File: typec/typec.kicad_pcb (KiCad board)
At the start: 2 copper layers, 17 parts, among them U1 TPD6E05U06-USON, U2 TPD4E05U06-USON, U3 TPS62081-WSON, U4 TPD4E05U06-USON, U5 TPS74801-VSON

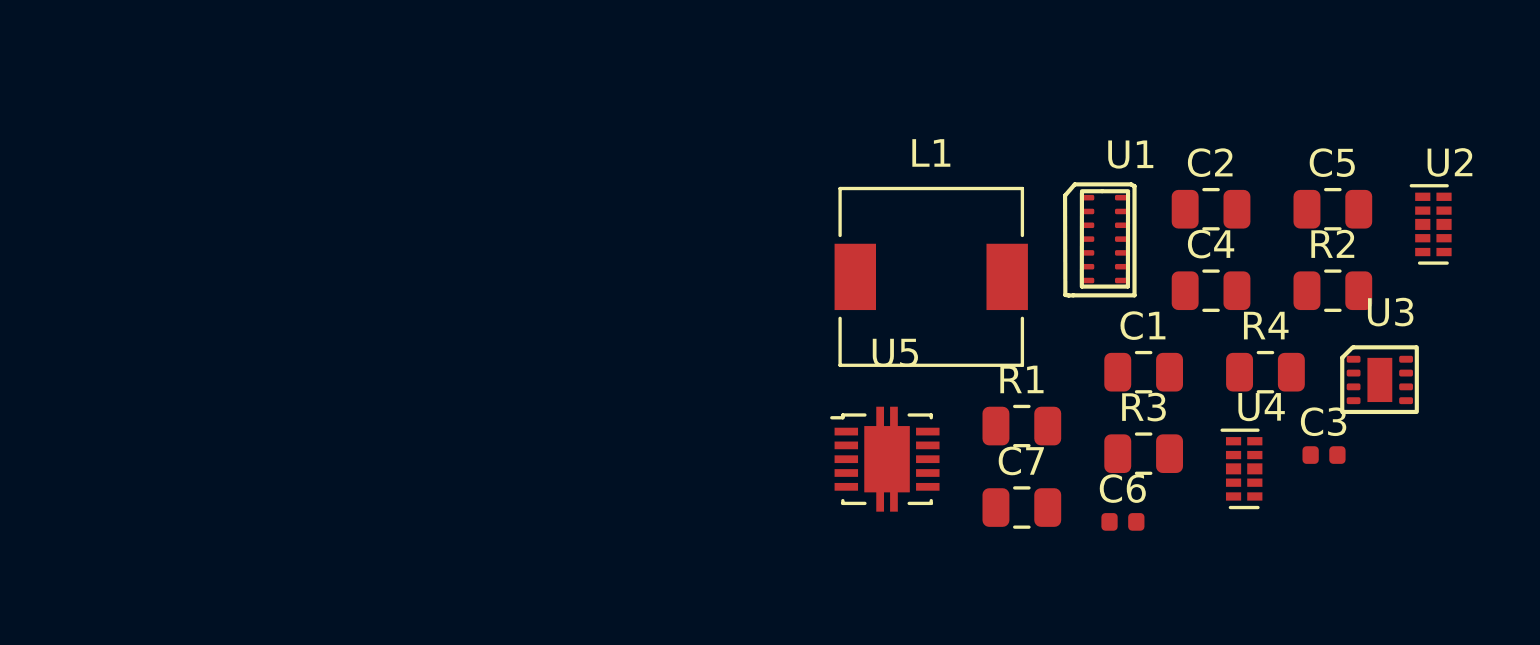
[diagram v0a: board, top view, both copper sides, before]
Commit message: Added TUSB212 and USB 3.1 Connector
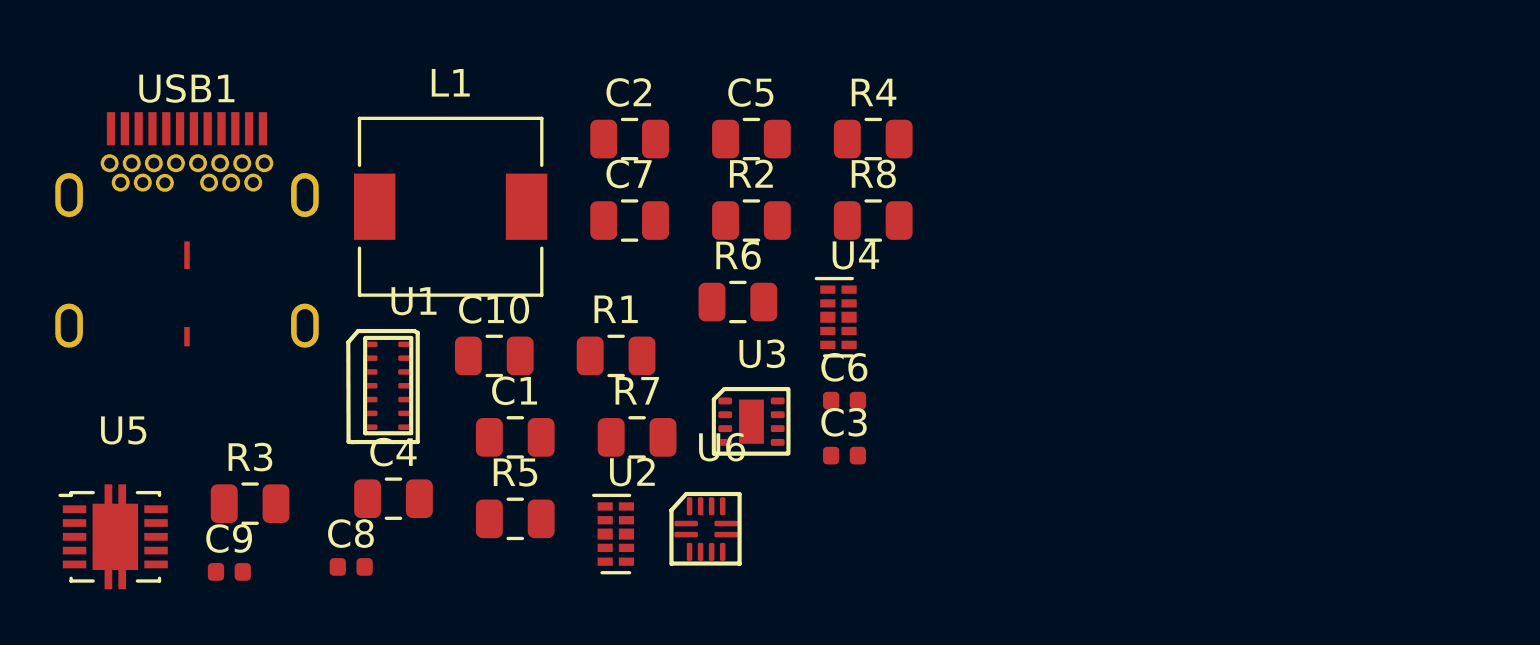
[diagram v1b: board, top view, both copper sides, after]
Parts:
- added C10: 10uf/10v, Capacitor_SMD:C_0805_2012Metric, F.Cu at (108.6, 96.5)
- added C8: 0.1uF/10v, Capacitor_SMD:C_0402_1005Metric, F.Cu at (103.4, 104.1)
- added C9: 0.1uF/10v, Capacitor_SMD:C_0402_1005Metric, F.Cu at (99.0, 104.3)
- added R5: 1.6K, Resistor_SMD:R_0805_2012Metric, F.Cu at (109.4, 102.4)
- added R6: 43K, Resistor_SMD:R_0805_2012Metric, F.Cu at (117.4, 94.5)
- added R7: 0 E, Resistor_SMD:R_0805_2012Metric, F.Cu at (113.8, 99.4)
- added R8: 0 E, Resistor_SMD:R_0805_2012Metric, F.Cu at (122.3, 91.6)
- added U6: TUSB212-X2QFN, TUSB212-X2QFN:TUSB212-X2QFN, F.Cu at (116.3, 102.7)
- added USB1: Wurth-632723300011, Type-C:Wurth-632723300011-MaximumExtensionMount, F.Cu at (97.5, 98.8)
- moved R3 32.4 mm to (99.8, 101.8)
- moved U2 31.7 mm to (112.7, 103.0)
- moved C4 30.5 mm to (105.0, 101.6)
- moved U5 28.1 mm to (94.4, 102.8)
- moved U1 26.5 mm to (104.8, 97.5)
- moved C1 22.9 mm to (109.4, 99.4)
- moved U3 22.8 mm to (117.6, 99.2)
- moved C2 21.2 mm to (113.5, 88.6)
- moved C5 21.2 mm to (117.9, 88.6)
- moved R2 21.2 mm to (117.9, 91.6)
- moved C7 17.6 mm to (113.5, 91.6)
- moved L1 17.6 mm to (107.0, 91.1)
- moved C3 17.4 mm to (121.3, 100.1)
- moved R4 16.5 mm to (122.3, 88.6)
- moved U4 15.7 mm to (120.7, 95.1)
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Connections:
- C7 pad 1: Net-(C7-Pad1) -> VOUT(3.3V)
- U3 pad 3: Net-(U3-Pad3) -> GND
- U3 pad 4: Net-(U3-Pad4) -> GND
- U3 pad 8: Net-(U3-Pad8) -> VBUS

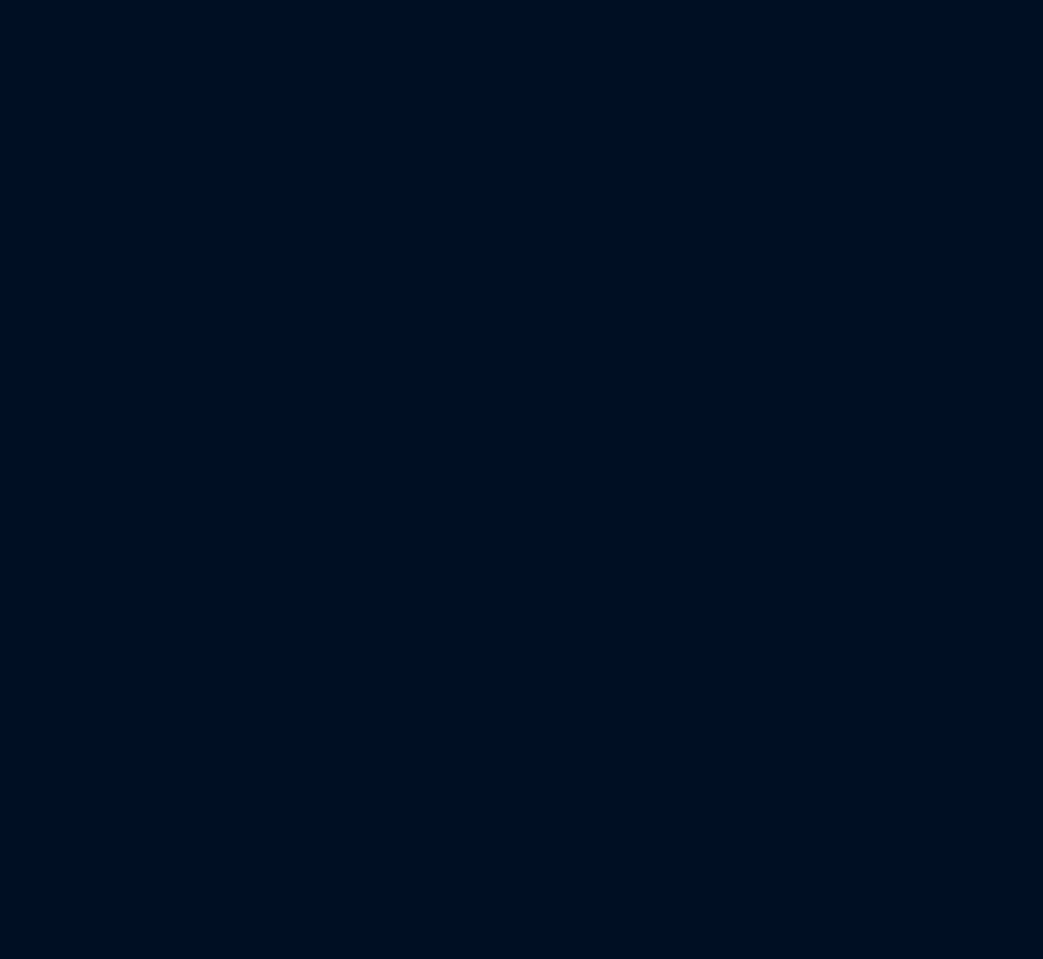
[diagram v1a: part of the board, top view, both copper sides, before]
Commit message: Added another page and completed the Multiplexer schematics.
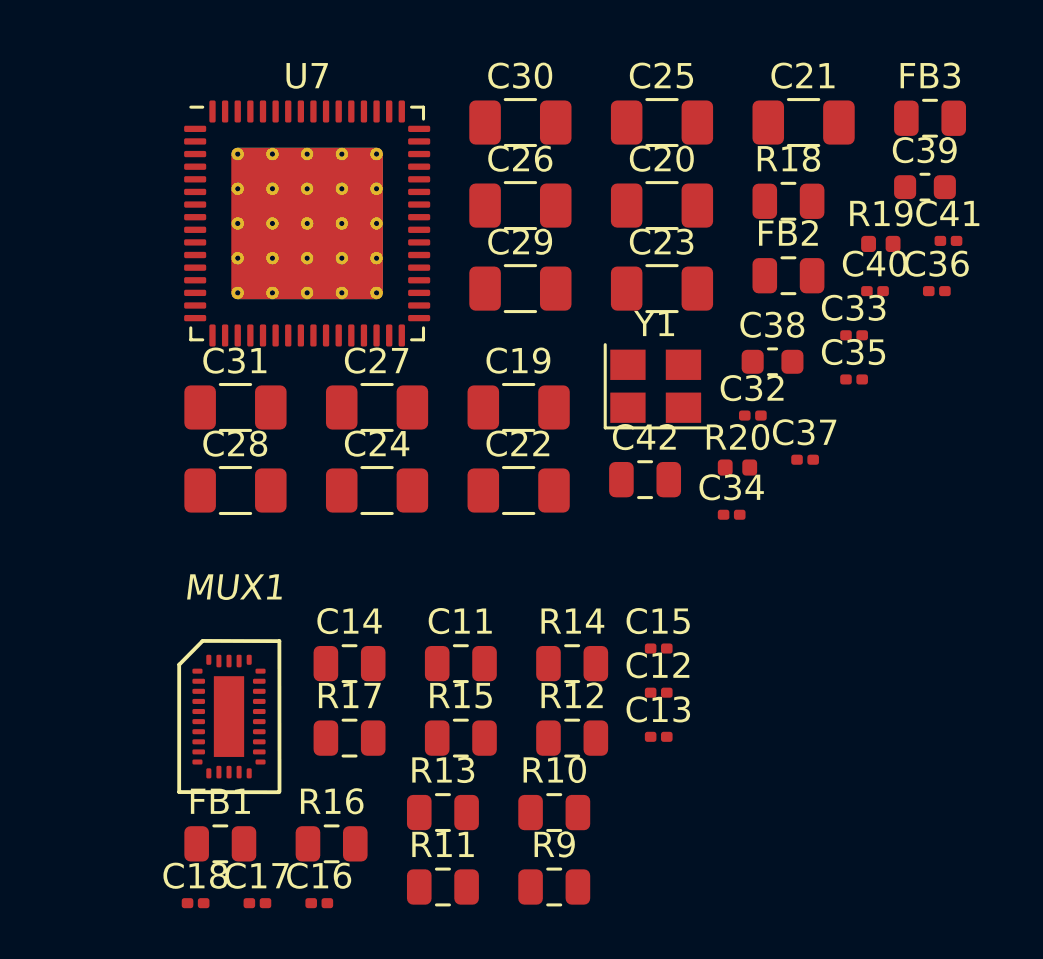
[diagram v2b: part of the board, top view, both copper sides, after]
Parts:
- added C11: 0.1uf/10v, Capacitor_SMD:C_0805_2012Metric, F.Cu at (152.2, 100.1)
- added C12: 0.47uf/10v, Capacitor_SMD:C_0201_0603Metric, F.Cu at (160.0, 101.2)
- added C13: 0.47uf/10v, Capacitor_SMD:C_0201_0603Metric, F.Cu at (160.0, 103.0)
- added C14: 47uf/10v, Capacitor_SMD:C_0805_2012Metric, F.Cu at (147.8, 100.1)
- added C15: 0.4uf/10v, Capacitor_SMD:C_0201_0603Metric, F.Cu at (160.0, 99.5)
- added C16: 0.47uf/10v, Capacitor_SMD:C_0201_0603Metric, F.Cu at (146.6, 109.5)
- added C17: 0.4uf/10v, Capacitor_SMD:C_0201_0603Metric, F.Cu at (144.1, 109.5)
- added C18: 0.4uf/10v, Capacitor_SMD:C_0201_0603Metric, F.Cu at (141.7, 109.5)
- added C19: 0.1uF/10v, Capacitor_SMD:C_1206_3216Metric, F.Cu at (154.5, 89.9)
- added C20: 0.1uF/10v, Capacitor_SMD:C_1206_3216Metric, F.Cu at (160.2, 81.9)
- added C21: 0.1uF/10v, Capacitor_SMD:C_1206_3216Metric, F.Cu at (165.8, 78.6)
- added C22: 0.1uF/10v, Capacitor_SMD:C_1206_3216Metric, F.Cu at (154.5, 93.2)
- added C23: 0.1uF/10v, Capacitor_SMD:C_1206_3216Metric, F.Cu at (160.2, 85.2)
- added C24: 0.1uF/10v, Capacitor_SMD:C_1206_3216Metric, F.Cu at (148.9, 93.2)
- added C25: 0.1uF/10v, Capacitor_SMD:C_1206_3216Metric, F.Cu at (160.2, 78.6)
- added C26: 10uF/10v, Capacitor_SMD:C_1206_3216Metric, F.Cu at (154.6, 81.9)
- added C27: 0.1uF/10v, Capacitor_SMD:C_1206_3216Metric, F.Cu at (148.9, 89.9)
- added C28: 0.1uF/10v, Capacitor_SMD:C_1206_3216Metric, F.Cu at (143.3, 93.2)
- added C29: 0.1uF/10v, Capacitor_SMD:C_1206_3216Metric, F.Cu at (154.6, 85.2)
- added C30: 0.1uF/10v, Capacitor_SMD:C_1206_3216Metric, F.Cu at (154.6, 78.6)
- added C31: 10uF/10v, Capacitor_SMD:C_1206_3216Metric, F.Cu at (143.3, 89.9)
- added C32: 0.1uF/10v, Capacitor_SMD:C_0201_0603Metric, F.Cu at (163.8, 90.2)
- added C33: 0.1uF/10v, Capacitor_SMD:C_0201_0603Metric, F.Cu at (167.8, 87.0)
- added C34: 0.1uF/10v, Capacitor_SMD:C_0201_0603Metric, F.Cu at (162.9, 94.2)
- added C35: 0.1uF/10v, Capacitor_SMD:C_0201_0603Metric, F.Cu at (167.8, 88.8)
- added C36: 0.1uF/10v, Capacitor_SMD:C_0201_0603Metric, F.Cu at (171.1, 85.3)
- added C37: 0.1uF/10v, Capacitor_SMD:C_0201_0603Metric, F.Cu at (165.8, 92.0)
- added C38: 18pF/10v, Capacitor_SMD:C_0603_1608Metric, F.Cu at (164.6, 88.1)
- added C39: 18pF/10v, Capacitor_SMD:C_0603_1608Metric, F.Cu at (170.6, 81.2)
- added C40: 0.1uF/10v, Capacitor_SMD:C_0201_0603Metric, F.Cu at (168.6, 85.3)
- added C41: 0.1uF/10v, Capacitor_SMD:C_0201_0603Metric, F.Cu at (171.5, 83.3)
- added C42: 1uF/10v, Capacitor_SMD:C_0805_2012Metric, F.Cu at (159.5, 92.8)
- added FB1: Ferrite_Bead, Inductor_SMD:L_0805_2012Metric, F.Cu at (142.7, 107.2)
- added FB2: Ferrite_Bead, Inductor_SMD:L_0805_2012Metric, F.Cu at (165.2, 84.7)
- added FB3: Ferrite_Bead, Inductor_SMD:L_0805_2012Metric, F.Cu at (170.8, 78.4)
- added MUX1: HD3SS3220, HD3SS3220-VQFN:HD3SS3220-VQFN-MUX, F.Cu at (143.0, 102.2)
- added R10: 10 K, Resistor_SMD:R_0805_2012Metric, F.Cu at (155.9, 106.0)
- added R11: 900 K, Resistor_SMD:R_0805_2012Metric, F.Cu at (151.5, 108.9)
- added R12: 100K, Resistor_SMD:R_0805_2012Metric, F.Cu at (156.6, 103.0)
- added R13: 4.7K, Resistor_SMD:R_0805_2012Metric, F.Cu at (151.5, 106.0)
- added R14: 100K, Resistor_SMD:R_0805_2012Metric, F.Cu at (156.6, 100.1)
- added R15: 100K, Resistor_SMD:R_0805_2012Metric, F.Cu at (152.2, 103.0)
- added R16: 0 E, Resistor_SMD:R_0805_2012Metric, F.Cu at (147.1, 107.2)
- added R17: 0 E, Resistor_SMD:R_0805_2012Metric, F.Cu at (147.8, 103.0)
- added R18: 1 M, Resistor_SMD:R_0805_2012Metric, F.Cu at (165.2, 81.7)
- added R19: 4.7K, Resistor_SMD:R_0402_1005Metric, F.Cu at (168.8, 83.4)
- added R20: 4.7K, Resistor_SMD:R_0402_1005Metric, F.Cu at (163.2, 92.3)
- added R9: 100K, Resistor_SMD:R_0805_2012Metric, F.Cu at (155.9, 108.9)
- added U7: USB_HUB, TUSB8042-VQFN:QFN-64-1EP_9x9mm_P0.5mm_EP6x6mm_ThermalVias, F.Cu at (146.1, 82.6)
- added Y1: 24 MHz, Crystal:Crystal_SMD_3225-4Pin_3.2x2.5mm, F.Cu at (159.9, 89.1)
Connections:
- net GND renamed USB3_RX0N
- USB1 pad 15: CRX2N -> CTX2N

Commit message: Last minute changes
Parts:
- moved C9 57.8 mm to (154.3, 87.4)
- moved C8 54.2 mm to (154.3, 85.4)
- moved C1 50.4 mm to (155.3, 78.9)
- moved R3 49.7 mm to (146.0, 83.8)
- moved C17 47.9 mm to (180.9, 78.8)
- moved C4 47.4 mm to (146.5, 78.9)
- moved C16 47.2 mm to (180.9, 77.1)
- moved FB1 46.8 mm to (177.5, 75.9)
- moved C10 43.1 mm to (146.5, 75.9)
- moved C25 42.9 mm to (133.6, 112.3)
- moved FB3 42.7 mm to (144.3, 111.8)
- moved C29 37.9 mm to (128.0, 112.3)
- moved C36 36.4 mm to (147.7, 113.2)
- moved L1 35.4 mm to (140.0, 78.4)
- moved C5 35.4 mm to (150.9, 75.9)
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
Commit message: updated
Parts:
- removed C37: 0.1uF/10v, Capacitor_SMD:C_0201_0603Metric
- removed C9: 0.1uF/10v, Capacitor_SMD:C_0402_1005Metric
- added C43: 1uF/10v, Capacitor_SMD:C_0603_1608Metric, F.Cu at (148.6, 66.8)
- added C44: 1uf/10v, Capacitor_SMD:C_0603_1608Metric, F.Cu at (153.8, 65.4)
- added C45: 1uf/10v, Capacitor_SMD:C_0603_1608Metric, F.Cu at (153.7, 67.3)
- added C46: 10 uF/10v, Capacitor_SMD:C_0603_1608Metric, F.Cu at (152.0, 69.0)
- added D1: LED, LED_SMD:LED_0402_1005Metric, F.Cu at (148.8, 54.7)
- added D10: LED, LED_SMD:LED_0402_1005Metric, F.Cu at (138.4, 93.6)
- added D11: LED, LED_SMD:LED_0402_1005Metric, F.Cu at (138.5, 91.3)
- added D12: LED, LED_SMD:LED_0402_1005Metric, F.Cu at (138.5, 89.3)
- added D2: LED, LED_SMD:LED_0402_1005Metric, F.Cu at (157.5, 51.3)
- added D3: LED, LED_SMD:LED_0402_1005Metric, F.Cu at (148.9, 53.0)
- added D4: LED, LED_SMD:LED_0402_1005Metric, F.Cu at (134.0, 64.8)
- added D5: LED, LED_SMD:LED_0402_1005Metric, F.Cu at (132.0, 38.0)
- added D6: LED, LED_SMD:LED_0402_1005Metric, F.Cu at (130.7, 52.5)
- added D7: LED, LED_SMD:LED_0402_1005Metric, F.Cu at (137.9, 52.1)
- added D8: LED, LED_SMD:LED_0402_1005Metric, F.Cu at (134.6, 60.6)
- added D9: LED, LED_SMD:LED_0402_1005Metric, F.Cu at (159.1, 72.9)
- added J1: Conn_01x05_Female, Connector_JST:JST_GH_SM05B-GHS-TB_1x05-1MP_P1.25mm_Horizontal, F.Cu at (117.3, 94.7)
- added J2: Conn_01x05_Female, Connector_JST:JST_GH_SM05B-GHS-TB_1x05-1MP_P1.25mm_Horizontal, F.Cu at (116.9, 57.5)
- added J3: Conn_01x05_Female, Connector_JST:JST_GH_SM05B-GHS-TB_1x05-1MP_P1.25mm_Horizontal, F.Cu at (117.2, 69.4)
- added J4: Conn_01x05_Female, Connector_JST:JST_GH_SM05B-GHS-TB_1x05-1MP_P1.25mm_Horizontal, F.Cu at (117.3, 81.8)
- added J5: Conn_01x05_Female, Connector_JST:JST_GH_SM05B-GHS-TB_1x05-1MP_P1.25mm_Horizontal, F.Cu at (131.9, 102.4)
- added J6: Conn_01x02_Female, Connector_PinHeader_1.00mm:PinHeader_1x02_P1.00mm_Vertical, F.Cu at (156.6, 95.9)
- added JP1: Jumper_NO_Small, Connector_PinHeader_1.00mm:PinHeader_1x02_P1.00mm_Vertical, F.Cu at (153.4, 48.8)
- added JP2: Jumper_NO_Small, Connector_PinHeader_1.00mm:PinHeader_1x02_P1.00mm_Vertical, F.Cu at (158.4, 48.7)
- added JP3: Jumper_3_Open, Connector_JST:JST_EH_B3B-EH-A_1x03_P2.50mm_Vertical, F.Cu at (161.8, 36.2)
- added JP4: Jumper_2_Open, Connector_PinHeader_1.00mm:PinHeader_1x02_P1.00mm_Vertical, F.Cu at (151.5, 63.4)
- added JP5: Jumper_2_Open, Connector_PinHeader_1.00mm:PinHeader_1x02_P1.00mm_Vertical, F.Cu at (146.6, 63.9)
- added JP6: Jumper_2_Open, Connector_PinHeader_1.00mm:PinHeader_1x02_P1.00mm_Vertical, F.Cu at (150.9, 60.7)
- added JP7: Jumper_2_Open, Connector_PinHeader_1.00mm:PinHeader_1x02_P1.00mm_Vertical, F.Cu at (148.0, 61.4)
- added JP8: Jumper_3_Open, Connector_JST:JST_EH_B3B-EH-A_1x03_P2.50mm_Vertical, F.Cu at (115.5, 38.7)
- added JP9: Jumper_3_Open, Connector_JST:JST_EH_B3B-EH-A_1x03_P2.50mm_Vertical, F.Cu at (116.3, 46.3)
- added R21: 0 E, Resistor_SMD:R_0201_0603Metric, F.Cu at (147.0, 55.1)
- added R22: 200 K, Resistor_SMD:R_0402_1005Metric, F.Cu at (138.1, 59.0)
- added R23: 500 E, Resistor_SMD:R_0402_1005Metric, F.Cu at (136.1, 51.9)
- added R25: 200 K, Resistor_SMD:R_0402_1005Metric, F.Cu at (151.4, 57.7)
- added R26: 500 E, Resistor_SMD:R_0402_1005Metric, F.Cu at (136.3, 60.2)
- added R27: NC / 10 K, Resistor_SMD:R_0402_1005Metric, F.Cu at (124.8, 67.5)
- added R28: NC/ 10 K, Resistor_SMD:R_0402_1005Metric, F.Cu at (125.5, 63.5)
- added R31: 330 E, Resistor_SMD:R_0402_1005Metric, F.Cu at (160.3, 73.9)
- added R34: 330 E, Resistor_SMD:R_0402_1005Metric, F.Cu at (141.2, 64.6)
- added R35: 330 E, Resistor_SMD:R_0402_1005Metric, F.Cu at (154.7, 74.2)
- added R36: 330 E, Resistor_SMD:R_0402_1005Metric, F.Cu at (135.2, 90.6)
- added R37: 1 K, Resistor_SMD:R_0402_1005Metric, F.Cu at (173.3, 75.3)
- added R38: 1 K, Resistor_SMD:R_0402_1005Metric, F.Cu at (172.6, 82.1)
- added R39: 1 K, Resistor_SMD:R_0402_1005Metric, F.Cu at (172.4, 84.6)
- added R40: 9.53 K, Resistor_SMD:R_0402_1005Metric, F.Cu at (139.8, 66.5)
- added R41: 1 K, Resistor_SMD:R_0402_1005Metric, F.Cu at (130.9, 89.5)
- added R43: 1 K, Resistor_SMD:R_0402_1005Metric, F.Cu at (172.5, 80.1)
- added R44: 1 M, Resistor_SMD:R_0402_1005Metric, F.Cu at (125.8, 80.6)
- added R45: 1 K, Resistor_SMD:R_0402_1005Metric, F.Cu at (180.0, 103.7)
- added R46: 1 K, Resistor_SMD:R_0402_1005Metric, F.Cu at (175.1, 103.6)
- added R47: 1 K, Resistor_SMD:R_0402_1005Metric, F.Cu at (177.6, 103.7)
- added R48: 10 K, Resistor_SMD:R_0402_1005Metric, F.Cu at (172.8, 58.7)
- added R49: 1 K, Resistor_SMD:R_0402_1005Metric, F.Cu at (172.9, 104.2)
- added R50: 10 K, Resistor_SMD:R_0402_1005Metric, F.Cu at (172.6, 61.3)
- added R51: 4.7 K, Resistor_SMD:R_0402_1005Metric, F.Cu at (169.9, 103.6)
- added R52: 10 K, Resistor_SMD:R_0402_1005Metric, F.Cu at (172.7, 63.8)
- added R53: 4.7 K, Resistor_SMD:R_0402_1005Metric, F.Cu at (167.4, 103.6)
- added R54: 90.9 K, Resistor_SMD:R_0402_1005Metric, F.Cu at (151.7, 70.9)
- added R55: 10 K, Resistor_SMD:R_0402_1005Metric, F.Cu at (172.7, 66.4)
- added R56: 10 K, Resistor_SMD:R_0402_1005Metric, F.Cu at (154.6, 69.3)
- added R57: 4.7 K, Resistor_SMD:R_0402_1005Metric, F.Cu at (165.0, 103.6)
- added R58: 4.7 K, Resistor_SMD:R_0402_1005Metric, F.Cu at (174.5, 64.6)
- added SW1: SW_Push_Dual_x2, Button_Switch_THT:SW_DIP_SPSTx01_Slide_6.7x4.1mm_W7.62mm_P2.54mm_LowProfile, F.Cu at (163.0, 47.7)
- added SW2: SW_DIP_x06, Button_Switch_THT:SW_DIP_SPSTx06_Slide_6.7x16.8mm_W7.62mm_P2.54mm_LowProfile, F.Cu at (162.5, 72.0)
- added SW4: SW_DIP_x08, Button_Switch_THT:SW_DIP_SPSTx08_Slide_6.7x21.88mm_W7.62mm_P2.54mm_LowProfile, F.Cu at (180.1, 93.9)
- added SW5: SW_DIP_x04, Button_Switch_THT:SW_DIP_SPSTx04_Slide_6.7x11.72mm_W7.62mm_P2.54mm_LowProfile, F.Cu at (162.6, 59.4)
- added TP1: TestPoint, TestPoint:TestPoint_THTPad_2.0x2.0mm_Drill1.0mm, F.Cu at (152.9, 35.3)
- added TP2: TestPoint, TestPoint:TestPoint_THTPad_2.0x2.0mm_Drill1.0mm, F.Cu at (125.9, 36.0)
- added TP3: TestPoint, TestPoint:TestPoint_THTPad_2.0x2.0mm_Drill1.0mm, F.Cu at (129.9, 60.5)
- added TP4: TestPoint, TestPoint:TestPoint_THTPad_2.0x2.0mm_Drill1.0mm, F.Cu at (128.8, 48.1)
- added TP5: TestPoint, TestPoint:TestPoint_THTPad_2.0x2.0mm_Drill1.0mm, F.Cu at (125.2, 51.1)
- added TP6: TestPoint, TestPoint:TestPoint_THTPad_2.0x2.0mm_Drill1.0mm, F.Cu at (178.4, 81.7)
- added TP7: TestPoint, TestPoint:TestPoint_THTPad_2.0x2.0mm_Drill1.0mm, F.Cu at (162.3, 104.3)
- added TP8: TestPoint, TestPoint:TestPoint_THTPad_2.0x2.0mm_Drill1.0mm, F.Cu at (128.1, 89.0)
- added e1: 105 K, Resistor_SMD:R_0201_0603Metric, F.Cu at (134.1, 67.5)
- C10: value 10uf/10v -> 0.1uf/10v; footprint Capacitor_SMD:C_0805_2012Metric -> Capacitor_SMD:C_0603_1608Metric
- C11: value 0.1uf/10v -> 0.47uf/10v; footprint Capacitor_SMD:C_0805_2012Metric -> Capacitor_SMD:C_0201_0603Metric
- C13: value 0.47uf/10v -> 4.7uf/10v; footprint Capacitor_SMD:C_0201_0603Metric -> Capacitor_SMD:C_0402_1005Metric
- C14: value 47uf/10v -> 0.4uf/10v; footprint Capacitor_SMD:C_0805_2012Metric -> Capacitor_SMD:C_0201_0603Metric
- C15: value 0.4uf/10v -> 0.47uf/10v
- C16: value 0.47uf/10v -> 0.4uf/10v
- C18: value 0.4uf/10v -> 10uF/10v; footprint Capacitor_SMD:C_0201_0603Metric -> Capacitor_SMD:C_0603_1608Metric
- C19, C20, C21, C22, C23, C24, C25, C28, C29, C30: footprint Capacitor_SMD:C_1206_3216Metric -> Capacitor_SMD:C_0402_1005Metric
- C2: value 10uf/10v -> 0.1uF/10v; footprint Capacitor_SMD:C_0805_2012Metric -> Capacitor_SMD:C_0402_1005Metric
- C26: value 10uF/10v -> 0.1uF/10v; footprint Capacitor_SMD:C_1206_3216Metric -> Capacitor_SMD:C_0603_1608Metric
- C27: footprint Capacitor_SMD:C_1206_3216Metric -> Capacitor_SMD:C_0603_1608Metric
- C3: value 1uf/10v -> 10uf/10v
- C31: value 10uF/10v -> 0.1uF/10v; footprint Capacitor_SMD:C_1206_3216Metric -> Capacitor_SMD:C_0402_1005Metric
- C32, C33: footprint Capacitor_SMD:C_0201_0603Metric -> Capacitor_SMD:C_0603_1608Metric
- C34: value 0.1uF/10v -> 10uF/10v; footprint Capacitor_SMD:C_0201_0603Metric -> Capacitor_SMD:C_0603_1608Metric
- C35, C41: footprint Capacitor_SMD:C_0201_0603Metric -> Capacitor_SMD:C_0402_1005Metric
- C36: value 0.1uF/10v -> 1uf/10v; footprint Capacitor_SMD:C_0201_0603Metric -> Capacitor_SMD:C_0603_1608Metric
- C38: value 18pF/10v -> 0.1uF/10v; footprint Capacitor_SMD:C_0603_1608Metric -> Capacitor_SMD:C_0402_1005Metric
- C39: footprint Capacitor_SMD:C_0603_1608Metric -> Capacitor_SMD:C_0402_1005Metric
- C4: value 10 uF/10V -> 1uf/10v; footprint Capacitor_SMD:C_0805_2012Metric -> Capacitor_SMD:C_0603_1608Metric
- C40: value 0.1uF/10v -> 18pF/10v; footprint Capacitor_SMD:C_0201_0603Metric -> Capacitor_SMD:C_0402_1005Metric
- C42: value 1uF/10v -> 0.1uF/10v; footprint Capacitor_SMD:C_0805_2012Metric -> Capacitor_SMD:C_0402_1005Metric
- C5: value 22uf/6.3v -> 10 uF/10V; footprint Capacitor_SMD:C_0805_2012Metric -> Capacitor_SMD:C_0603_1608Metric
- C6: value 560pf/10v -> 590pf/10v; footprint Capacitor_SMD:C_0402_1005Metric -> Capacitor_SMD:C_0201_0603Metric
- C7: value 10uf/10v -> 22uf/6.3v; footprint Capacitor_SMD:C_0805_2012Metric -> Capacitor_SMD:C_0603_1608Metric
- C8: value 0.1uF/10v -> 10uf/10v; footprint Capacitor_SMD:C_0402_1005Metric -> Capacitor_SMD:C_0603_1608Metric
- L1: footprint Inductor_SMD:L_6.3x6.3_H3 -> Inductor_SMD:L_Wuerth_MAPI-3015
- R1: value 105 K -> 1.6K; footprint Resistor_SMD:R_0805_2012Metric -> Resistor_SMD:R_0201_0603Metric
- R10: value 10 K -> 1.9K; footprint Resistor_SMD:R_0805_2012Metric -> Resistor_SMD:R_0402_1005Metric
- R11: value 900 K -> 330 E; footprint Resistor_SMD:R_0805_2012Metric -> Resistor_SMD:R_0402_1005Metric
- R12, R15: footprint Resistor_SMD:R_0805_2012Metric -> Resistor_SMD:R_0201_0603Metric
- R13: value 4.7K -> 10 K; footprint Resistor_SMD:R_0805_2012Metric -> Resistor_SMD:R_0402_1005Metric
- R14: value 100K -> 900 K; footprint Resistor_SMD:R_0805_2012Metric -> Resistor_SMD:R_0402_1005Metric
- R16: value 0 E -> 4.7K; footprint Resistor_SMD:R_0805_2012Metric -> Resistor_SMD:R_0402_1005Metric
- R17: value 0 E -> 100K; footprint Resistor_SMD:R_0805_2012Metric -> Resistor_SMD:R_0402_1005Metric
- R18: value 1 M -> 100K; footprint Resistor_SMD:R_0805_2012Metric -> Resistor_SMD:R_0402_1005Metric
- R19: value 4.7K -> 200 K
- R2: value 178K -> 330 E; footprint Resistor_SMD:R_0805_2012Metric -> Resistor_SMD:R_0402_1005Metric
- R20: value 4.7K -> 0 E
- R3: value 5 K -> 330 E; footprint Resistor_SMD:R_0805_2012Metric -> Resistor_SMD:R_0201_0603Metric
- R4: value 1.9K -> 43K; footprint Resistor_SMD:R_0805_2012Metric -> Resistor_SMD:R_0201_0603Metric
- R5: value 1.6K -> 100 E; footprint Resistor_SMD:R_0805_2012Metric -> Resistor_SMD:R_0402_1005Metric
- R6: value 43K -> 330 E; footprint Resistor_SMD:R_0805_2012Metric -> Resistor_SMD:R_0402_1005Metric
- R7: value 0 E -> 178K; footprint Resistor_SMD:R_0805_2012Metric -> Resistor_SMD:R_0402_1005Metric
- R8: value 0 E -> 5 K; footprint Resistor_SMD:R_0805_2012Metric -> Resistor_SMD:R_0402_1005Metric
- R9: value 100K -> 330 E; footprint Resistor_SMD:R_0805_2012Metric -> Resistor_SMD:R_0402_1005Metric
- U2: value TPD4E05U06-USON -> TUSB212-X2QFN; footprint TPD4E05U06-USON:TPD4E05U06-USON -> TUSB212-X2QFN:TUSB212-X2QFN
- U3: value TPS62081-WSON -> TPD4E05U06-USON; footprint TPS62081-WSON:TPS62081-WSON -> TPD4E05U06-USON:TPD4E05U06-USON
- U5: value TPS74801-VSON -> TPS62082-WSON; footprint TPS74801-VSON:TPS74801-VSON -> TPS62081-WSON:TPS62082-WSON
- U6: value TUSB212-X2QFN -> TPS74801-VSON; footprint TUSB212-X2QFN:TUSB212-X2QFN -> TPS74801-VSON:TPS74801-VSON
- moved R9 58.1 mm to (132.0, 40.0), turned to 90 degrees
- moved R19 57.9 mm to (137.4, 54.4), turned to 270 degrees
- moved C8 54.0 mm to (132.8, 35.8)
- moved USB1 53.6 mm to (145.8, 34.7), turned to 180 degrees
- moved U5 52.8 mm to (135.0, 37.9), turned to 270 degrees
- moved C7 51.9 mm to (139.5, 37.1), turned to 270 degrees
- moved R11 51.5 mm to (132.7, 52.0)
- moved FB1 51.4 mm to (133.2, 49.7)
- moved C22 49.2 mm to (151.2, 65.6), turned to 180 degrees
- moved C19 48.5 mm to (137.4, 63.8)
- moved R20 48.4 mm to (138.4, 56.6)
- moved R7 48.4 mm to (134.2, 40.7), turned to 180 degrees
- moved C16 47.8 mm to (141.7, 49.8), turned to 90 degrees
- moved R10 46.6 mm to (131.7, 70.0), turned to 180 degrees
- moved C25 46.1 mm to (137.4, 66.3)
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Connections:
- C1 pad 1: VOUT(1.1V) -> VBUS
- C1 pad 2: USB3_RX0N -> GND
- C10 pad 1: VBUS -> Net-(C10-Pad1)
- C10 pad 2: USB3_RX0N -> GND
- C12 pad 2: USB3_RX0N -> USB3_RX0P
- C13 pad 1: Net-(C13-Pad1) -> GND
- C13 pad 2: USB3_RX0N -> VBUS
- C14 pad 1: USB3_RX0N -> CTX1N0
- C14 pad 2: VBUS -> Net-(C14-Pad2)
- C15 pad 1: CTX1N -> Net-(C15-Pad1)
- C15 pad 2: Net-(C15-Pad2) -> CTX2P0
- C16 pad 2: CTX2P -> CTX2N0
- C17 pad 2: CTX2N -> CTX1P0
- C18 pad 2: CTX1P -> GND
- C19 pad 1: USB3_RX0N -> GND
- C19 pad 2: Net-(C19-Pad2) -> Net-(C18-Pad1)
- C2 pad 1: VBUS -> Net-(C2-Pad1)
- C2 pad 2: USB3_RX0N -> GND
- C20 pad 1: USB3_RX0N -> GND
- C20 pad 2: Net-(C19-Pad2) -> Net-(C18-Pad1)
- C21 pad 1: USB3_RX0N -> GND
- C21 pad 2: Net-(C19-Pad2) -> Net-(C18-Pad1)
- C22 pad 1: USB3_RX0N -> GND
- C22 pad 2: Net-(C19-Pad2) -> Net-(C18-Pad1)
- C23 pad 1: USB3_RX0N -> GND
- C23 pad 2: Net-(C19-Pad2) -> Net-(C18-Pad1)
- C24 pad 1: USB3_RX0N -> GND
- C24 pad 2: Net-(C19-Pad2) -> Net-(C18-Pad1)
- C25 pad 1: USB3_RX0N -> GND
- C25 pad 2: Net-(C19-Pad2) -> Net-(C18-Pad1)
- C26 pad 1: Net-(C19-Pad2) -> GND
- C26 pad 2: USB3_RX0N -> Net-(C26-Pad2)
- C27 pad 1: USB3_RX0N -> GND
- C27 pad 2: Net-(C27-Pad2) -> Net-(C26-Pad2)
- C28 pad 1: USB3_RX0N -> (no net)
- C28 pad 2: Net-(C27-Pad2) -> Net-(C28-Pad2)
- C29 pad 1: USB3_RX0N -> Net-(C29-Pad1)
- C29 pad 2: Net-(C27-Pad2) -> (no net)
- C3 pad 1: Net-(C3-Pad1) -> VOUT(1.1V)
- C3 pad 2: USB3_RX0N -> GND
- C30 pad 1: USB3_RX0N -> (no net)
- C30 pad 2: Net-(C27-Pad2) -> Net-(C30-Pad2)
- C31 pad 1: Net-(C27-Pad2) -> Net-(C31-Pad1)
- C31 pad 2: USB3_RX0N -> (no net)
- C32 pad 1: Tx1+ -> GND
- C32 pad 2: Net-(C32-Pad2) -> Net-(C26-Pad2)
- C33 pad 1: Net-(C33-Pad1) -> GND
- C33 pad 2: Tx1- -> Net-(C26-Pad2)
- C34 pad 1: Tx2+ -> Net-(C26-Pad2)
- C34 pad 2: Net-(C34-Pad2) -> GND
- C35 pad 1: Net-(C35-Pad1) -> (no net)
- C35 pad 2: Tx2- -> Net-(C35-Pad2)
- C36 pad 1: Tx3+ -> VOUT(3.3V)
- C36 pad 2: Net-(C36-Pad2) -> GND
- C38 pad 2: USB3_RX0N -> (no net)
- C39 pad 1: USB3_RX0N -> Net-(C39-Pad1)
- C39 pad 2: Net-(C39-Pad2) -> GND
- C4 pad 1: VBUS -> VOUT(3.3V)
- C4 pad 2: USB3_RX0N -> GND
- C40 pad 1: Tx4+ -> GND
- C41 pad 1: Net-(C41-Pad1) -> (no net)
- C41 pad 2: Tx4- -> Net-(C41-Pad2)
- C42 pad 2: USB3_RX0N -> (no net)
- C5 pad 1: VOUT(3.3V) -> VBUS
- C5 pad 2: USB3_RX0N -> GND
- C6 pad 2: USB3_RX0N -> GND
- C7 pad 2: USB3_RX0N -> GND
- C8 pad 1: USB3_RX0N -> VOUT(3.3V)
- C8 pad 2: Net-(C8-Pad2) -> GND
- FB1 pad 2: Net-(C11-Pad1) -> Net-(C10-Pad1)
- FB2 pad 2: Net-(C19-Pad2) -> Net-(C18-Pad1)
- FB3 pad 2: Net-(C27-Pad2) -> Net-(C26-Pad2)
- MUX1 pad 1: CC2 -> CC20
- MUX1 pad 10: Net-(C13-Pad1) -> Net-(C12-Pad1)
- MUX1 pad 11: Net-(MUX1-Pad11) -> DIR
- MUX1 pad 13: USB3_RX0N -> GND
- MUX1 pad 14: CRX1N -> CRX1N0
- MUX1 pad 15: CRX1P -> CRX1P0
- MUX1 pad 16: Net-(C15-Pad2) -> Net-(C14-Pad2)
- MUX1 pad 17: Net-(C18-Pad1) -> Net-(C17-Pad1)
- MUX1 pad 18: CRX2N -> CRX2N0
- MUX1 pad 19: CRX2P -> CRX2P0
- MUX1 pad 2: CC1 -> CC10
- MUX1 pad 20: Net-(C17-Pad1) -> Net-(C16-Pad1)
- MUX1 pad 21: Net-(C16-Pad1) -> Net-(C15-Pad1)
- MUX1 pad 22: Net-(MUX1-Pad22) -> ADDR
- MUX1 pad 23: Net-(MUX1-Pad23) -> INT_NOUT3
- MUX1 pad 24: Net-(MUX1-Pad24) -> (no net)
- MUX1 pad 25: Net-(MUX1-Pad25) -> SDAOUT1
- MUX1 pad 26: Net-(MUX1-Pad26) -> SCLOUT2
- MUX1 pad 28: USB3_RX0N -> GND
- MUX1 pad 31: (no net) -> GND
- MUX1 pad 8: Net-(C11-Pad1) -> Net-(C10-Pad1)
- MUX1 pad 9: Net-(C12-Pad1) -> Net-(C11-Pad1)
- R1 pad 1: VOUT(1.1V) -> Net-(R1-Pad1)
- R1 pad 2: Net-(R1-Pad2) -> GND
- R10 pad 1: Net-(MUX1-Pad3) -> VOUT(1.1V)
- R10 pad 2: VBUS -> Net-(R10-Pad2)
- R11 pad 1: Net-(MUX1-Pad5) -> VOUT(3.3V)
- R11 pad 2: VBUS -> Net-(D6-Pad2)
- R12 pad 1: USB3_RX0N -> USB3_TX0N
- R12 pad 2: USB3_TX0P -> GND
- R13 pad 1: Net-(MUX1-Pad4) -> Net-(MUX1-Pad3)
- R13 pad 2: USB3_RX0N -> VBUS
- R14 pad 1: USB3_RX0N -> Net-(MUX1-Pad5)
- R14 pad 2: USB3_RX0N -> VBUS
- R15 pad 1: USB3_RX0N -> GND
- R15 pad 2: USB3_RX0N -> USB3_TX0P
- R16 pad 1: USB3_RX0N -> Net-(JP3-Pad2)
- R16 pad 2: Net-(MUX1-Pad29) -> Net-(MUX1-Pad4)
- R17 pad 1: Net-(MUX1-Pad12) -> USB3_RX0N
- R17 pad 2: USB3_RX0N -> GND
- R18 pad 1: Net-(C38-Pad1) -> USB3_RX0P
- R18 pad 2: Net-(C39-Pad2) -> GND
- R19 pad 1: USB3_RX0N -> Net-(MUX1-Pad27)
- R19 pad 2: Net-(R19-Pad2) -> VBUS
- R2 pad 1: Net-(R2-Pad1) -> VBUS
- R2 pad 2: VOUT(3.3V) -> Net-(D1-Pad2)
- R20 pad 1: USB3_RX0N -> GND
- R20 pad 2: Net-(R20-Pad2) -> Net-(MUX1-Pad29)
- R3 pad 1: USB3_RX0N -> VOUT(3.3V)
- R3 pad 2: Net-(R3-Pad2) -> Net-(D2-Pad2)
- R4 pad 1: VOUT(1.1V) -> VOUT(3.3V)
- R4 pad 2: Net-(R3-Pad2) -> Net-(R4-Pad2)
- R5 pad 1: Net-(R5-Pad1) -> SCL
- R5 pad 2: USB3_RX0N -> Net-(D3-Pad2)
- R6 pad 2: Net-(R6-Pad2) -> Net-(D4-Pad2)
- R7 pad 1: CC1 -> Net-(R7-Pad1)
- R7 pad 2: Net-(R7-Pad2) -> VOUT(3.3V)
- R8 pad 1: CC2 -> GND
- R8 pad 2: Net-(R8-Pad2) -> Net-(R10-Pad2)
- R9 pad 1: USB3_TX0N -> VOUT(3.3V)
- R9 pad 2: USB3_RX0N -> Net-(D5-Pad2)
- U1 pad 10: USB3_RX0N -> GND
- U1 pad 13: CC2 -> (no net)
- U1 pad 14: CC1 -> CC10
- U1 pad 2: CC2 -> CSBU2
- U1 pad 3: USB2_N0 -> USB2_N
- U1 pad 4: USB2_P0 -> USB2_P
- U1 pad 5: USB3_RX0N -> GND
- U1 pad 6: CSBU2 -> CC2
- U1 pad 8: CSBU1 -> (no net)
- U1 pad 9: CSBU2 -> CC20
- U2 pad 1: CTX1N -> USB2_N0
- U2 pad 10: CTX1N -> GND
- U2 pad 2: CTX1P -> USB2_P0
- U2 pad 3: USB3_RX0N -> Net-(JP1-Pad2)
- U2 pad 4: CRX1N -> SCL
- U2 pad 5: CRX1P -> Net-(SW1-Pad2)
- U2 pad 6: CRX1P -> Net-(R1-Pad1)
- U2 pad 7: CRX1N -> USB2_P10
- U2 pad 8: USB3_RX0N -> USB2_N10
- U2 pad 9: CTX1P -> Net-(R4-Pad2)
- U3 pad 1: VBUS -> CRX1N
- U3 pad 2: USB3_RX0N -> CRX1P
- U3 pad 3: USB3_RX0N -> GND
- U3 pad 4: USB3_RX0N -> CTX1P
- U3 pad 5: VOUT(3.3V) -> CTX1N
- U3 pad 6: Net-(R2-Pad1) -> CTX1N0
- U3 pad 7: Net-(L1-Pad1) -> CTX1P0
- U3 pad 8: VBUS -> GND
- U3 pad 9: (no net) -> CRX1P0
- U4 pad 1: CTX2N -> CRX2N
- U4 pad 10: CTX2N -> CRX2N0
- U4 pad 2: CTX2P -> CRX2P
- U4 pad 3: USB3_RX0N -> GND
- U4 pad 4: CRX2N -> CTX2P
- U4 pad 5: CRX2P -> CTX2N
- U4 pad 6: CRX2P -> CTX2N0
- U4 pad 7: CRX2N -> CTX2P0
- U4 pad 8: USB3_RX0N -> GND
- U4 pad 9: CTX2P -> CRX2P0
- U5 pad 2: VBUS -> GND
- U5 pad 3: Net-(R1-Pad2) -> GND
- U5 pad 4: Net-(C3-Pad1) -> GND
- U5 pad 5: Net-(C3-Pad1) -> VOUT(3.3V)
- U5 pad 6: USB3_RX0N -> Net-(R7-Pad1)
- U5 pad 7: Net-(C6-Pad1) -> Net-(L1-Pad1)
- U5 pad 8: Net-(R3-Pad2) -> VBUS
- U5 pad 9: VOUT(1.1V) -> GND
- U6 pad 1: USB2_N0 -> VOUT(3.3V)
- U6 pad 10: Net-(C9-Pad2) -> VOUT(1.1V)
- U6 pad 11: Net-(C9-Pad1) -> GND
- U6 pad 2: USB2_P0 -> VOUT(3.3V)
- U6 pad 4: Net-(U6-Pad4) -> VOUT(3.3V)
- U6 pad 5: Net-(C8-Pad2) -> VOUT(3.3V)
- U6 pad 6: Net-(R5-Pad1) -> GND
- U6 pad 7: USB2_P0 -> Net-(C6-Pad1)
- U6 pad 8: USB2_N0 -> Net-(R10-Pad2)
- U6 pad 9: Net-(R6-Pad2) -> VOUT(1.1V)
- U7 pad 11: Net-(C34-Pad2) -> Net-(C30-Pad2)
- U7 pad 12: Net-(C35-Pad1) -> Net-(C31-Pad1)
- U7 pad 13: Net-(C19-Pad2) -> Net-(C18-Pad1)
- U7 pad 14: Rx2+ -> (no net)
- U7 pad 15: Rx2- -> (no net)
- U7 pad 16: Net-(C27-Pad2) -> Net-(C26-Pad2)
- U7 pad 19: Net-(C36-Pad2) -> Net-(C35-Pad2)
- U7 pad 20: Net-(C37-Pad1) -> Net-(C38-Pad1)
- U7 pad 21: Net-(C19-Pad2) -> Net-(C18-Pad1)
- U7 pad 22: Rx3+ -> (no net)
- U7 pad 23: Rx3- -> (no net)
- U7 pad 26: Net-(C40-Pad2) -> Net-(C41-Pad2)
- U7 pad 27: Net-(C41-Pad1) -> Net-(C42-Pad1)
- U7 pad 28: Net-(C19-Pad2) -> Net-(C18-Pad1)
- U7 pad 29: Rx4+ -> (no net)
- U7 pad 3: Net-(C32-Pad2) -> Net-(C28-Pad2)
- U7 pad 30: Rx4- -> (no net)
- U7 pad 31: Net-(C19-Pad2) -> Net-(C18-Pad1)
- U7 pad 32: Net-(U7-Pad32) -> PWRON4_BATEN4
- U7 pad 33: Net-(U7-Pad33) -> PWRON3_BATEN3
- U7 pad 34: Net-(C27-Pad2) -> Net-(C26-Pad2)
- U7 pad 35: Net-(U7-Pad35) -> PWRON2_BATEN2
- U7 pad 36: Net-(U7-Pad36) -> PWRON1_BATEN1
- U7 pad 37: Net-(U7-Pad37) -> SDA_SMBDAT
- U7 pad 38: Net-(U7-Pad38) -> SCL_SMBCLK
- U7 pad 39: Net-(U7-Pad39) -> SMBUSZ
- U7 pad 4: Net-(C33-Pad1) -> Net-(C29-Pad1)
- U7 pad 40: Net-(R19-Pad2) -> FULLPWRMGMTZ_SS_UP
- U7 pad 41: Net-(U7-Pad41) -> PWRCTL_POL_TDO
- U7 pad 42: Net-(R20-Pad2) -> GANGED_HS_UP
- U7 pad 43: Net-(U7-Pad43) -> OVERCUR4z
- U7 pad 44: Net-(U7-Pad44) -> OVERCUR3z
- U7 pad 45: Net-(U7-Pad45) -> AUTOENZ
- U7 pad 46: Net-(U7-Pad46) -> OVERCUR1z
- U7 pad 47: Net-(U7-Pad47) -> OVERCUR2z
- U7 pad 49: Net-(U7-Pad49) -> TEST_TRSTZ
- U7 pad 5: Net-(C19-Pad2) -> Net-(C18-Pad1)
- U7 pad 50: Net-(C42-Pad1) -> Net-(C43-Pad1)
- U7 pad 51: Net-(C19-Pad2) -> Net-(C18-Pad1)
- U7 pad 52: Net-(C27-Pad2) -> Net-(C26-Pad2)
- U7 pad 55: Net-(U7-Pad55) -> USB3_TX0P
- U7 pad 56: Net-(U7-Pad56) -> USB3_TX0N
- U7 pad 57: Net-(C19-Pad2) -> Net-(C18-Pad1)
- U7 pad 58: Net-(U7-Pad58) -> USB3_RX0P
- U7 pad 59: Net-(U7-Pad59) -> USB3_RX0N
- U7 pad 6: Rx1+ -> (no net)
- U7 pad 60: Net-(U7-Pad60) -> (no net)
- U7 pad 61: Net-(C38-Pad1) -> Net-(C39-Pad1)
- U7 pad 62: Net-(C39-Pad2) -> Net-(C40-Pad2)
- U7 pad 63: Net-(C27-Pad2) -> Net-(C26-Pad2)
- U7 pad 65: (no net) -> GND
- U7 pad 7: Rx1- -> (no net)
- U7 pad 8: Net-(C19-Pad2) -> Net-(C18-Pad1)
- USB1 pad 1: USB3_RX0N -> GND
- USB1 pad 12: USB3_RX0N -> GND
- USB1 pad 13: USB3_RX0N -> GND
- USB1 pad 17: Net-(R8-Pad2) -> CC2
- USB1 pad 18: USB2_P0 -> USB2_P
- USB1 pad 19: USB2_N0 -> USB2_N
- USB1 pad 24: USB3_RX0N -> GND
- USB1 pad 25: Net-(USB1-Pad25) -> GND
- USB1 pad 26: Net-(USB1-Pad26) -> GND
- USB1 pad 27: Net-(USB1-Pad27) -> GND
- USB1 pad 5: Net-(R7-Pad2) -> CC1
- USB1 pad 6: USB2_N0 -> USB2_N
- USB1 pad 7: USB2_P0 -> USB2_P
- Y1 pad 1: Net-(C39-Pad2) -> Net-(C40-Pad2)
- Y1 pad 2: Net-(C38-Pad1) -> Net-(C39-Pad1)
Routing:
- net GND: track 0.00 -> 789.0 mm, vias 0 -> 21
- net VBUS: track 0.00 -> 720.6 mm, vias 0 -> 10
- net VOUT(3.3V): track 0.00 -> 490.6 mm, vias 0 -> 6
- net Net-(C18-Pad1): track 0.00 -> 116.5 mm, vias 0 -> 2
- net Net-(R41-Pad2): track 0.00 -> 72.1 mm, vias 0 -> 1
- net Net-(C26-Pad2): track 0.00 -> 69.7 mm, vias 0 -> 7
- net Net-(R58-Pad1): track 0.00 -> 57.7 mm, vias 0 -> 2
- net TEST_TRSTZ: track 0.00 -> 56.9 mm, vias 0 -> 1
- net SCL_SMBCLK: track 0.00 -> 55.8 mm, vias 0 -> 1
- net SDA_SMBDAT: track 0.00 -> 52.6 mm, vias 0 -> 1
- net Net-(J2-Pad2): track 0.00 -> 48.4 mm, vias 0 -> 1
- net Net-(C39-Pad1): track 0.00 -> 46.3 mm, vias 0 -> 4
- net ADDR: track 0.00 -> 41.7 mm, vias 0 -> 2
- net SMBUSZ: track 0.00 -> 40.1 mm
- net Net-(J2-Pad3): track 0.00 -> 38.2 mm, vias 0 -> 1
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- added copper zone on B.Cu, net (none)
- added copper zone on F.Cu, net (none)
- added copper zone on In1.Cu, net (none)
- added copper zone on In2.Cu, net (none)
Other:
- board outline added: 70.3 x 73.3 mm
- copper layers 2 -> 4
